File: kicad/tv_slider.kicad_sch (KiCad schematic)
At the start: 10 parts, among them J1 MC 1,5/2-G-3.81, J2 MC 1,5/6-G-3.81, J3 MC 1,5/4-G-3.81, J4 MC 1,5/3-G-3.81, J5 MC 1,5/3-G-3.81, J6 MC 1,5/3-G-3.81, J7 MC 1,5/3-G-3.81

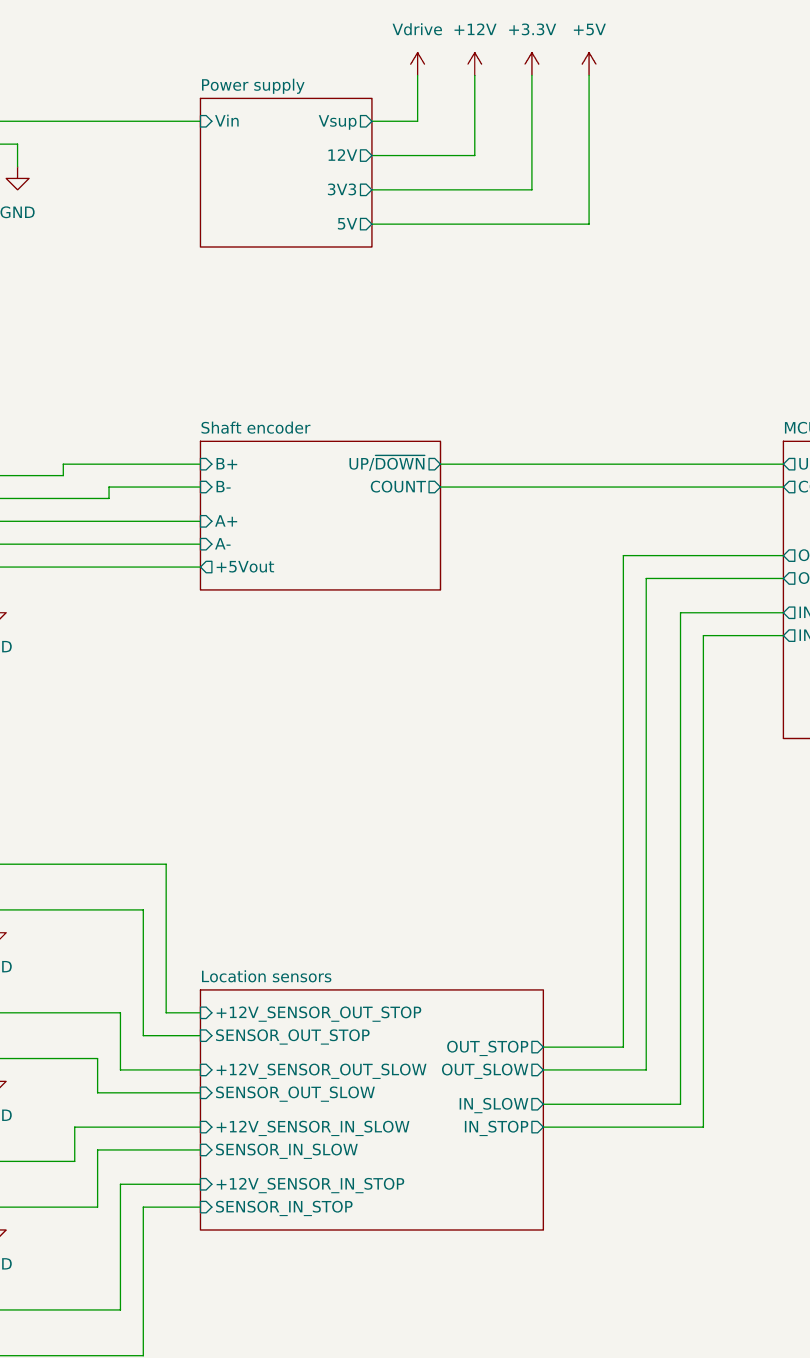
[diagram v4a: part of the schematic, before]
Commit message: Finished the schematic and started the PCB.
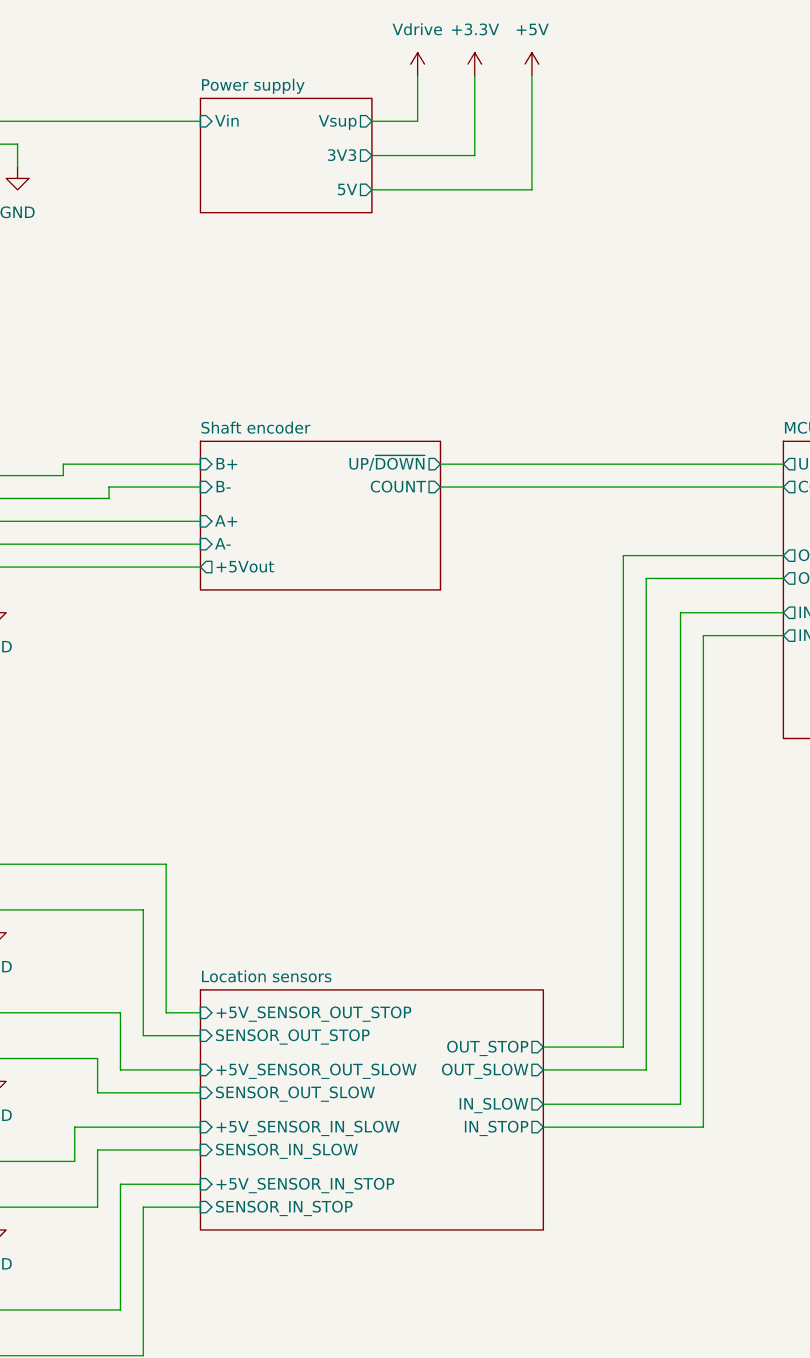
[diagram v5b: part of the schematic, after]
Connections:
- net Location sensors/+12V_SENSOR_IN_SLOW renamed Location sensors/+5V_SENSOR_IN_SLOW
- net Location sensors/+12V_SENSOR_IN_STOP renamed Location sensors/+5V_SENSOR_IN_STOP
- net Location sensors/+12V_SENSOR_OUT_SLOW renamed Location sensors/+5V_SENSOR_OUT_SLOW
- net Location sensors/+12V_SENSOR_OUT_STOP renamed Location sensors/+5V_SENSOR_OUT_STOP
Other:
- sheet Location sensors ports: added +5V_SENSOR_IN_SLOW, +5V_SENSOR_IN_STOP, +5V_SENSOR_OUT_SLOW, +5V_SENSOR_OUT_STOP; removed +12V_SENSOR_IN_SLOW, +12V_SENSOR_IN_STOP, +12V_SENSOR_OUT_SLOW, +12V_SENSOR_OUT_STOP
- sheet Power supply ports: added none; removed 12V
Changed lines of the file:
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@@
+	(wire
+		(pts
+			(xy 106.68 39.37) (xy 95.25 39.37)
+		)
+		(stroke
+			(width 0)
+			(type default)
+		)
+	)
+	(wire
+		(pts
+			(xy 53.34 120.65) (xy 53.34 124.46)
+		)
+		(stroke
+			(width 0)
+			(type default)
+		)
+	)
+	(wire
+		(pts
+			(xy 231.14 80.01) (xy 240.03 80.01)
+		)
+		(stroke
+			(width 0)
+			(type default)
+		)
+	)
+	(wire
+		(pts
+			(xy 132.08 92.71) (xy 132.08 147.32)
+		)
+		(stroke
+			(width 0)
+			(type default)
+		)
+	)
 	(wire
 		(pts
@@
 	(wire
 		(pts
-			(xy 53.34 120.65) (xy 53.34 124.46)
-		)
-		(stroke
-			(width 0)
-			(type default)
-		)
-	)
-	(wire
-		(pts
-			(xy 231.14 80.01) (xy 240.03 80.01)
-		)
-		(stroke
-			(width 0)
-			(type default)
-		)
-	)
-	(wire
-		(pts
-			(xy 132.08 92.71) (xy 132.08 147.32)
-		)
-		(stroke
-			(width 0)
-			(type default)
-		)
-	)
-	(wire
-		(pts
-			(xy 119.38 46.99) (xy 95.25 46.99)
-		)
-		(stroke
-			(width 0)
-			(type default)
-		)
-	)
-	(wire
-		(pts
-			(xy 119.38 30.48) (xy 119.38 46.99)
+			(xy 113.03 30.48) (xy 113.03 43.18)
 		)
 		(stroke
@@
 	(wire
 		(pts
+			(xy 129.54 90.17) (xy 140.97 90.17)
+		)
+		(stroke
+			(width 0)
+			(type default)
+		)
+	)
+	(wire
+		(pts
+			(xy 53.34 170.18) (xy 52.07 170.18)
+		)
+		(stroke
+			(width 0)
+			(type default)
+		)
+	)
+	(wire
+		(pts
+			(xy 53.34 137.16) (xy 52.07 137.16)
+		)
+		(stroke
+			(width 0)
+			(type default)
+		)
+	)
+	(wire
+		(pts
+			(xy 240.03 80.01) (xy 240.03 81.28)
+		)
+		(stroke
+			(width 0)
+			(type default)
+		)
+	)
+	(wire
+		(pts
 			(xy 106.68 30.48) (xy 106.68 39.37)
 		)
@@
 	(wire
 		(pts
-			(xy 129.54 90.17) (xy 140.97 90.17)
-		)
-		(stroke
-			(width 0)
-			(type default)
-		)
-	)
-	(wire
-		(pts
-			(xy 53.34 170.18) (xy 52.07 170.18)
-		)
-		(stroke
-			(width 0)
-			(type default)
-		)
-	)
-	(wire
-		(pts
-			(xy 53.34 137.16) (xy 52.07 137.16)
-		)
-		(stroke
-			(width 0)
-			(type default)
-		)
-	)
-	(wire
-		(pts
-			(xy 240.03 80.01) (xy 240.03 81.28)
-		)
-		(stroke
-			(width 0)
-			(type default)
-		)
-	)
-	(wire
-		(pts
-			(xy 113.03 30.48) (xy 113.03 43.18)
-		)
-		(stroke
-			(width 0)
-			(type default)
-		)
-	)
-	(wire
-		(pts
 			(xy 231.14 82.55) (xy 236.22 82.55)
 		)
@@
 		(pts
 			(xy 72.39 134.62) (xy 76.2 134.62)
-		)
-		(stroke
-			(width 0)
-			(type default)
-		)
-	)
-	(wire
-		(pts
-			(xy 106.68 39.37) (xy 95.25 39.37)
 		)
 		(stroke
@@
 		(dnp no)
 		(fields_autoplaced yes)
-		(property "Reference" "#PWR07"
+		(property "Reference" "#PWR06"
 			(at 53.34 130.81 0)
 			(effects
@@
 			(project "tv_slider"
 				(path "/914c4b67-a7a4-47f3-8515-668040fd3f8c"
-					(reference "#PWR07")
+					(reference "#PWR06")
 					(unit 1)
 				)
@@
 	(symbol
 		(lib_id "power:+5V")
-		(at 119.38 30.48 0)
+		(at 113.03 30.48 0)
 		(unit 1)
 		(exclude_from_sim no)
@@
 		(dnp no)
 		(fields_autoplaced yes)
-		(property "Reference" "#PWR04"
-			(at 119.38 34.29 0)
+		(property "Reference" "#PWR03"
+			(at 113.03 34.29 0)
 			(effects
 				(font
@@
 		)
 		(property "Value" "+5V"
-			(at 119.38 25.4 0)
+			(at 113.03 25.4 0)
 			(effects
 				(font
@@
 		)
 		(property "Footprint" ""
-			(at 119.38 30.48 0)
+			(at 113.03 30.48 0)
 			(effects
 				(font
@@
 		)
 		(property "Datasheet" ""
-			(at 119.38 30.48 0)
+			(at 113.03 30.48 0)
 			(effects
 				(font
@@
 		)
 		(property "Description" "Power symbol creates a global label with name \"+5V\""
-			(at 119.38 30.48 0)
+			(at 113.03 30.48 0)
 			(effects
 				(font
@@
 			(project ""
 				(path "/914c4b67-a7a4-47f3-8515-668040fd3f8c"
-					(reference "#PWR04")
+					(reference "#PWR03")
 					(unit 1)
 				)
@@
 		(dnp no)
 		(fields_autoplaced yes)
-		(property "Reference" "#PWR09"
+		(property "Reference" "#PWR08"
 			(at 53.34 163.83 0)
 			(effects
@@
 			(project "tv_slider"
 				(path "/914c4b67-a7a4-47f3-8515-668040fd3f8c"
-					(reference "#PWR09")
+					(reference "#PWR08")
 					(unit 1)
 				)
@@
 		(dnp no)
 		(fields_autoplaced yes)
-		(property "Reference" "#PWR08"
+		(property "Reference" "#PWR07"
 			(at 53.34 147.32 0)
 			(effects
@@
 			(project "tv_slider"
 				(path "/914c4b67-a7a4-47f3-8515-668040fd3f8c"
-					(reference "#PWR08")
+					(reference "#PWR07")
 					(unit 1)
 				)
@@
 		(dnp no)
 		(fields_autoplaced yes)
-		(property "Reference" "#PWR06"
+		(property "Reference" "#PWR05"
 			(at 53.34 95.25 0)
 			(effects
@@
 			(project "tv_slider"
 				(path "/914c4b67-a7a4-47f3-8515-668040fd3f8c"
-					(reference "#PWR06")
+					(reference "#PWR05")
 					(unit 1)
 				)
@@
 		(dnp no)
 		(fields_autoplaced yes)
-		(property "Reference" "#PWR05"
+		(property "Reference" "#PWR04"
 			(at 55.88 46.99 0)
 			(effects
@@
 			(project ""
 				(path "/914c4b67-a7a4-47f3-8515-668040fd3f8c"
-					(reference "#PWR05")
+					(reference "#PWR04")
 					(unit 1)
 				)
@@
 	(symbol
 		(lib_id "power:+3.3V")
-		(at 113.03 30.48 0)
-		(unit 1)
-		(exclude_from_sim no)
-		(in_bom yes)
-		(on_board yes)
-		(dnp no)
-		(fields_autoplaced yes)
-		(property "Reference" "#PWR03"
-			(at 113.03 34.29 0)
-			(effects
-				(font
-					(size 1.27 1.27)
-				)
-				(hide yes)
-			)
-		)
-		(property "Value" "+3.3V"
-			(at 113.03 25.4 0)
-			(effects
-				(font
-					(size 1.27 1.27)
-				)
-			)
-		)
-		(property "Footprint" ""
-			(at 113.03 30.48 0)
-			(effects
-				(font
-					(size 1.27 1.27)
-				)
-				(hide yes)
-			)
-		)
-		(property "Datasheet" ""
-			(at 113.03 30.48 0)
-			(effects
-				(font
-					(size 1.27 1.27)
-				)
-				(hide yes)
-			)
-		)
-		(property "Description" "Power symbol creates a global label with name \"+3.3V\""
-			(at 113.03 30.48 0)
-			(effects
-				(font
-					(size 1.27 1.27)
-				)
-				(hide yes)
-			)
-		)
-		(pin "1"
-		)
-		(instances
-			(project ""
-				(path "/914c4b67-a7a4-47f3-8515-668040fd3f8c"
-					(reference "#PWR03")
-					(unit 1)
-				)
-			)
-		)
-	)
-	(symbol
-		(lib_id "power:+12V")
 		(at 106.68 30.48 0)
 		(unit 1)
@@
 			)
 		)
-		(property "Value" "+12V"
+		(property "Value" "+3.3V"
 			(at 106.68 25.4 0)
 			(effects
@@
 			)
 		)
-		(property "Description" "Power symbol creates a global label with name \"+12V\""
+		(property "Description" "Power symbol creates a global label with name \"+3.3V\""
 			(at 106.68 30.48 0)
 			(effects
@@
 		(dnp no)
 		(fields_autoplaced yes)
-		(property "Reference" "#PWR010"
+		(property "Reference" "#PWR09"
 			(at 53.34 180.34 0)
 			(effects
@@
 			(project "tv_slider"
 				(path "/914c4b67-a7a4-47f3-8515-668040fd3f8c"
-					(reference "#PWR010")
+					(reference "#PWR09")
 					(unit 1)
 				)
@@
 	(sheet
 		(at 76.2 33.02)
-		(size 19.05 16.51)
+		(size 19.05 12.7)
 		(exclude_from_sim no)
 		(in_bom yes)
@@
 		)
 		(property "Sheetfile" "power_supply.kicad_sch"
-			(at 76.2 50.1146 0)
+			(at 76.2 46.3046 0)
 			(effects
 				(font
@@
 		)
 		(pin "3V3" output
-			(at 95.25 43.18 0)
-			(effects
-				(font
-					(size 1.27 1.27)
-				)
-				(justify right)
-			)
-		)
-		(pin "12V" output
 			(at 95.25 39.37 0)
 			(effects
@@
 		)
 		(pin "5V" output
-			(at 95.25 46.99 0)
+			(at 95.25 43.18 0)
 			(effects
 				(font
@@
 			)
 		)
-		(pin "+12V_SENSOR_IN_SLOW" input
+		(pin "+5V_SENSOR_IN_SLOW" input
 			(at 76.2 147.32 180)
 			(effects
@@
 			)
 		)
-		(pin "+12V_SENSOR_IN_STOP" input
+		(pin "+5V_SENSOR_IN_STOP" input
 			(at 76.2 153.67 180)
 			(effects
@@
 			)
 		)
-		(pin "+12V_SENSOR_OUT_SLOW" input
+		(pin "+5V_SENSOR_OUT_SLOW" input
 			(at 76.2 140.97 180)
 			(effects
@@
 			)
 		)
-		(pin "+12V_SENSOR_OUT_STOP" input
+		(pin "+5V_SENSOR_OUT_STOP" input
 			(at 76.2 134.62 180)
 			(effects

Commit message: Completed the PCB design. Ready for final review.
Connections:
- net Motor drive/A+: now also J3.1 (Pin_1); no longer J3.4 (Pin_4)
- net Motor drive/A-: now also J3.2 (Pin_2); no longer J3.3 (Pin_3)
- net Motor drive/B+: now also J3.4 (Pin_4); no longer J3.2 (Pin_2)
- net Motor drive/B-: now also J3.3 (Pin_3); no longer J3.1 (Pin_1)
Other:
- sheet MCU ports: added none; removed ~{HOME}
- sheet Motor drive ports: added none; removed ~{HOME}
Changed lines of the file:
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@@
 	(title_block
 		(title "TV slider")
-		(date "2025-10-06")
-		(rev "1")
+		(date "2025-12-23")
+		(rev "1.0")
 		(company "NX Solutions")
 	)
@@
 	(wire
 		(pts
-			(xy 165.1 101.6) (xy 194.31 101.6)
-		)
-		(stroke
-			(width 0)
-			(type default)
-		)
-	)
-	(wire
-		(pts
 			(xy 64.77 149.86) (xy 64.77 156.21)
 		)
@@
 	(wire
 		(pts
-			(xy 231.14 90.17) (xy 240.03 90.17)
+			(xy 53.34 87.63) (xy 52.07 87.63)
 		)
 		(stroke
@@
 	(wire
 		(pts
-			(xy 53.34 87.63) (xy 52.07 87.63)
+			(xy 100.33 35.56) (xy 95.25 35.56)
 		)
 		(stroke
@@
 	(wire
 		(pts
-			(xy 100.33 35.56) (xy 95.25 35.56)
+			(xy 52.07 118.11) (xy 72.39 118.11)
 		)
 		(stroke
@@
 	(wire
 		(pts
-			(xy 52.07 118.11) (xy 72.39 118.11)
+			(xy 53.34 35.56) (xy 76.2 35.56)
 		)
 		(stroke
@@
 	(wire
 		(pts
-			(xy 53.34 35.56) (xy 76.2 35.56)
+			(xy 52.07 139.7) (xy 64.77 139.7)
 		)
 		(stroke
@@
 	(wire
 		(pts
-			(xy 52.07 139.7) (xy 64.77 139.7)
+			(xy 76.2 147.32) (xy 62.23 147.32)
 		)
 		(stroke
@@
 	(wire
 		(pts
-			(xy 76.2 147.32) (xy 62.23 147.32)
+			(xy 165.1 99.06) (xy 194.31 99.06)
 		)
 		(stroke
@@
 	(wire
 		(pts
-			(xy 165.1 99.06) (xy 194.31 99.06)
+			(xy 231.14 87.63) (xy 236.22 87.63)
+		)
+		(stroke
+			(width 0)
+			(type default)
+		)
+	)
+	(wire
+		(pts
+			(xy 231.14 90.17) (xy 240.03 90.17)
 		)
 		(stroke
@@
 	(wire
 		(pts
-			(xy 236.22 86.36) (xy 236.22 87.63)
+			(xy 236.22 87.63) (xy 236.22 86.36)
 		)
 		(stroke
@@
 	(wire
 		(pts
-			(xy 231.14 87.63) (xy 236.22 87.63)
-		)
-		(stroke
-			(width 0)
-			(type default)
-		)
-	)
-	(wire
-		(pts
 			(xy 100.33 30.48) (xy 100.33 35.56)
 		)
@@
 	)
 	(symbol
+		(lib_id "power:+3V3")
+		(at 106.68 30.48 0)
+		(unit 1)
+		(exclude_from_sim no)
+		(in_bom yes)
+		(on_board yes)
+		(dnp no)
+		(fields_autoplaced yes)
+		(property "Reference" "#PWR02"
+			(at 106.68 34.29 0)
+			(effects
+				(font
+					(size 1.27 1.27)
+				)
+				(hide yes)
+			)
+		)
+		(property "Value" "+3V3"
+			(at 106.68 25.4 0)
+			(effects
+				(font
+					(size 1.27 1.27)
+				)
+			)
+		)
+		(property "Footprint" ""
+			(at 106.68 30.48 0)
+			(effects
+				(font
+					(size 1.27 1.27)
+				)
+				(hide yes)
+			)
+		)
+		(property "Datasheet" ""
+			(at 106.68 30.48 0)
+			(effects
+				(font
+					(size 1.27 1.27)
+				)
+				(hide yes)
+			)
+		)
+		(property "Description" "Power symbol creates a global label with name \"+3V3\""
+			(at 106.68 30.48 0)
+			(effects
+				(font
+					(size 1.27 1.27)
+				)
+				(hide yes)
+			)
+		)
+		(pin "1"
+		)
+		(instances
+			(project ""
+				(path "/914c4b67-a7a4-47f3-8515-668040fd3f8c"
+					(reference "#PWR02")
+					(unit 1)
+				)
+			)
+		)
+	)
+	(symbol
 		(lib_id "Mechanical:Fiducial")
 		(at 269.24 161.29 0)
@@
 	(symbol
 		(lib_id "Connector_Generic:Conn_01x04")
-		(at 248.92 86.36 0)
-		(mirror x)
+		(at 248.92 83.82 0)
 		(unit 1)
 		(exclude_from_sim no)
@@
 		(dnp no)
 		(property "Reference" "J3"
-			(at 251.46 86.3601 0)
+			(at 251.46 83.8199 0)
 			(effects
 				(font
@@
 		)
 		(property "Value" "MC 1,5/4-G-3.81"
-			(at 251.46 83.8201 0)
+			(at 251.46 86.3599 0)
 			(effects
 				(font
@@
 		)
 		(property "Footprint" "Connector_Phoenix_MC:PhoenixContact_MC_1,5_4-G-3.81_1x04_P3.81mm_Horizontal"
-			(at 248.92 86.36 0)
+			(at 248.92 83.82 0)
 			(effects
 				(font
@@
 		)
 		(property "Datasheet" "~"
-			(at 248.92 86.36 0)
+			(at 248.92 83.82 0)
 			(effects
 				(font
@@
 		)
 		(property "Description" "Generic connector, single row, 01x04, script generated (kicad-library-utils/schlib/autogen/connector/)"
-			(at 248.92 86.36 0)
+			(at 248.92 83.82 0)
 			(effects
 				(font
@@
 		)
 		(property "Dielectric" ""
-			(at 248.92 86.36 0)
+			(at 248.92 83.82 0)
 			(effects
 				(font
@@
 		)
 		(property "Supplier" "Digi-Key"
-			(at 248.92 86.36 0)
+			(at 248.92 83.82 0)
 			(effects
 				(font
@@
 		)
 		(property "SupplierPN" "277-1208-ND"
-			(at 248.92 86.36 0)
+			(at 248.92 83.82 0)
 			(effects
 				(font
@@
 		)
 		(property "MF" "Phoenix"
-			(at 248.92 86.36 0)
+			(at 248.92 83.82 0)
 			(effects
 				(font
@@
 	)
 	(symbol
-		(lib_id "power:+3.3V")
-		(at 106.68 30.48 0)
-		(unit 1)
-		(exclude_from_sim no)
-		(in_bom yes)
-		(on_board yes)
-		(dnp no)
-		(fields_autoplaced yes)
-		(property "Reference" "#PWR02"
-			(at 106.68 34.29 0)
-			(effects
-				(font
-					(size 1.27 1.27)
-				)
-				(hide yes)
-			)
-		)
-		(property "Value" "+3.3V"
-			(at 106.68 25.4 0)
-			(effects
-				(font
-					(size 1.27 1.27)
-				)
-			)
-		)
-		(property "Footprint" ""
-			(at 106.68 30.48 0)
-			(effects
-				(font
-					(size 1.27 1.27)
-				)
-				(hide yes)
-			)
-		)
-		(property "Datasheet" ""
-			(at 106.68 30.48 0)
-			(effects
-				(font
-					(size 1.27 1.27)
-				)
-				(hide yes)
-			)
-		)
-		(property "Description" "Power symbol creates a global label with name \"+3.3V\""
-			(at 106.68 30.48 0)
-			(effects
-				(font
-					(size 1.27 1.27)
-				)
-				(hide yes)
-			)
-		)
-		(pin "1"
-		)
-		(instances
-			(project ""
-				(path "/914c4b67-a7a4-47f3-8515-668040fd3f8c"
-					(reference "#PWR02")
-					(unit 1)
-				)
-			)
-		)
-	)
-	(symbol
 		(lib_id "Connector_Generic:Conn_01x03")
 		(at 46.99 137.16 0)
@@
 	(sheet
 		(at 140.97 71.12)
-		(size 24.13 33.02)
+		(size 24.13 30.48)
 		(exclude_from_sim no)
 		(in_bom yes)
@@
 		)
 		(property "Sheetfile" "mcu.kicad_sch"
-			(at 140.97 104.7246 0)
+			(at 140.97 102.1846 0)
 			(effects
 				(font
@@
 			)
 		)
-		(pin "~{HOME}" input
-			(at 165.1 101.6 0)
-			(effects
-				(font
-					(size 1.27 1.27)
-				)
-				(justify right)
-			)
-		)
 		(instances
 			(project "tv_slider"
@@
 	(sheet
 		(at 194.31 71.12)
-		(size 36.83 33.02)
+		(size 36.83 30.48)
 		(exclude_from_sim no)
 		(in_bom yes)
@@
 		)
 		(property "Sheetfile" "motor_drive.kicad_sch"
-			(at 194.31 104.7246 0)
+			(at 194.31 102.1846 0)
 			(effects
 				(font
@@
 		)
 		(pin "B+" output
-			(at 231.14 87.63 0)
+			(at 231.14 90.17 0)
 			(effects
 				(font
@@
 		)
 		(pin "B-" output
-			(at 231.14 90.17 0)
+			(at 231.14 87.63 0)
 			(effects
 				(font
@@
 			(effects
 				(font
-					(size 1.27 1.27)
-				)
-				(justify left)
-			)
-		)
-		(pin "~{HOME}" output
-			(at 194.31 101.6 180)
-			(effects
-				(font

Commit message: Reviewed the part numbers, footprints and pin numbers.
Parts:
- J1: MP (none) -> 1803277; SupplierPN 277-1207-ND -> 277-1206-ND
- J2: MP (none) -> 1803316
- J3: MP (none) -> 1803293
- J4, J5, J6, J7: MP (none) -> 1803280
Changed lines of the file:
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@@
+			)
+		)
+		(property "SNAPEDA_PN" ""
+			(at 255.27 161.29 0)
+			(effects
+				(font
+					(size 1.27 1.27)
+				)
+				(hide yes)
 			)
 		)
@@
 			)
 		)
+		(property "SNAPEDA_PN" ""
+			(at 46.99 120.65 0)
+			(effects
+				(font
+					(size 1.27 1.27)
+				)
+				(hide yes)
+			)
+		)
+		(property "MP" "1803280"
+			(at 46.99 120.65 0)
+			(effects
+				(font
+					(size 1.27 1.27)
+				)
+				(hide yes)
+			)
+		)
 		(pin "1"
 		)
@@
 			)
 		)
+		(property "SNAPEDA_PN" ""
+			(at 269.24 161.29 0)
+			(effects
+				(font
+					(size 1.27 1.27)
+				)
+				(hide yes)
+			)
+		)
 		(instances
 			(project "tv_slider"
@@
 			)
 		)
+		(property "SNAPEDA_PN" ""
+			(at 241.3 161.29 0)
+			(effects
+				(font
+					(size 1.27 1.27)
+				)
+				(hide yes)
+			)
+		)
 		(instances
 			(project ""
@@
 			)
 		)
+		(property "SNAPEDA_PN" ""
+			(at 46.99 153.67 0)
+			(effects
+				(font
+					(size 1.27 1.27)
+				)
+				(hide yes)
+			)
+		)
+		(property "MP" "1803280"
+			(at 46.99 153.67 0)
+			(effects
+				(font
+					(size 1.27 1.27)
+				)
+				(hide yes)
+			)
+		)
 		(pin "1"
 		)
@@
 			)
 		)
+		(property "SNAPEDA_PN" ""
+			(at 248.92 83.82 0)
+			(effects
+				(font
+					(size 1.27 1.27)
+				)
+				(hide yes)
+			)
+		)
+		(property "MP" "1803293"
+			(at 248.92 83.82 0)
+			(effects
+				(font
+					(size 1.27 1.27)
+				)
+				(hide yes)
+			)
+		)
 		(pin "3"
 		)
@@
 			)
 		)
+		(property "SNAPEDA_PN" ""
+			(at 46.99 170.18 0)
+			(effects
+				(font
+					(size 1.27 1.27)
+				)
+				(hide yes)
+			)
+		)
+		(property "MP" "1803280"
+			(at 46.99 170.18 0)
+			(effects
+				(font
+					(size 1.27 1.27)
+				)
+				(hide yes)
+			)
+		)
 		(pin "1"
 		)
@@
 			)
 		)
+		(property "SNAPEDA_PN" ""
+			(at 46.99 82.55 0)
+			(effects
+				(font
+					(size 1.27 1.27)
+				)
+				(hide yes)
+			)
+		)
+		(property "MP" "1803316"
+			(at 46.99 82.55 0)
+			(effects
+				(font
+					(size 1.27 1.27)
+				)
+				(hide yes)
+			)
+		)
 		(pin "2"
 		)
@@
 			)
 		)
-		(property "SupplierPN" "277-1207-ND"
+		(property "SupplierPN" "277-1206-ND"
 			(at 48.26 38.1 0)
 			(effects
@@
 		)
 		(property "MF" "Phoenix"
+			(at 48.26 38.1 0)
+			(effects
+				(font
+					(size 1.27 1.27)
+				)
+				(hide yes)
+			)
+		)
+		(property "SNAPEDA_PN" ""
+			(at 48.26 38.1 0)
+			(effects
+				(font
+					(size 1.27 1.27)
+				)
+				(hide yes)
+			)
+		)
+		(property "MP" "1803277"
 			(at 48.26 38.1 0)
 			(effects
@@
 			(at 46.99 137.16 0)
 			(effects
+				(font
+					(size 1.27 1.27)
+				)
+				(hide yes)
+			)
+		)
+		(property "SNAPEDA_PN" ""
+			(at 46.99 137.16 0)
+			(effects
+				(font
+					(size 1.27 1.27)
+				)
+				(hide yes)
+			)
+		)
+		(property "MP" "1803280"
+			(at 46.99 137.16 0)
+			(effects
